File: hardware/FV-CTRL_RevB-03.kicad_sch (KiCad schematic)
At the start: 12 parts, among them J20 SMA 50ohm ANT, Y1 40MHz CL10pF

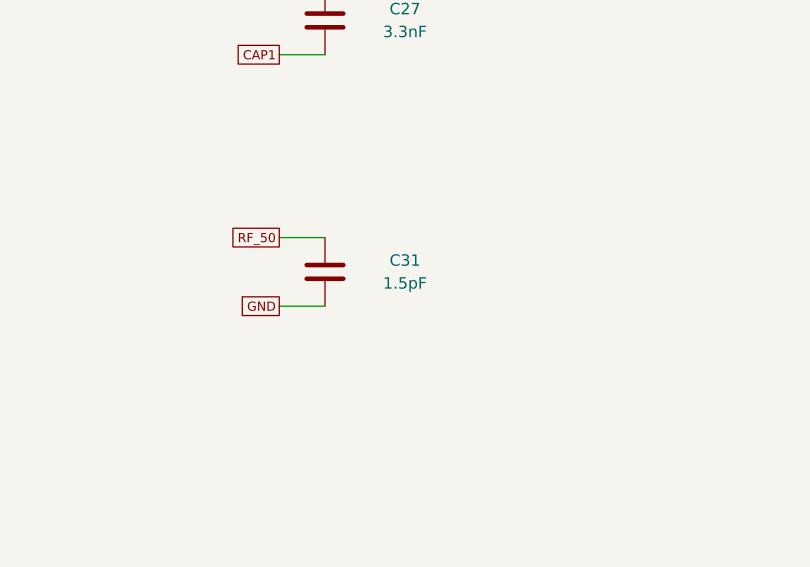
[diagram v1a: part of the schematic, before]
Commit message: fix(hardware): increase flash brownout margin and account for RF ESD capacitance
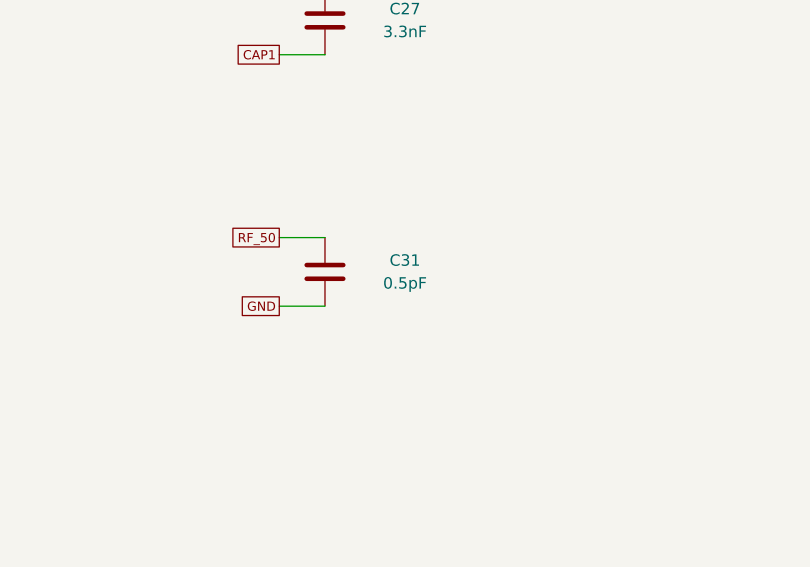
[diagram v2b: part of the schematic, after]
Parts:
- C31: value 1.5pF -> 0.5pF
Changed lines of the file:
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@@
 			(effects (font (size 1.27 1.27)))
 		)
-		(property "Value" "1.5pF"
+		(property "Value" "0.5pF"
 			(at 161.2900 97.7900 0)
 			(effects (font (size 1.27 1.27)))

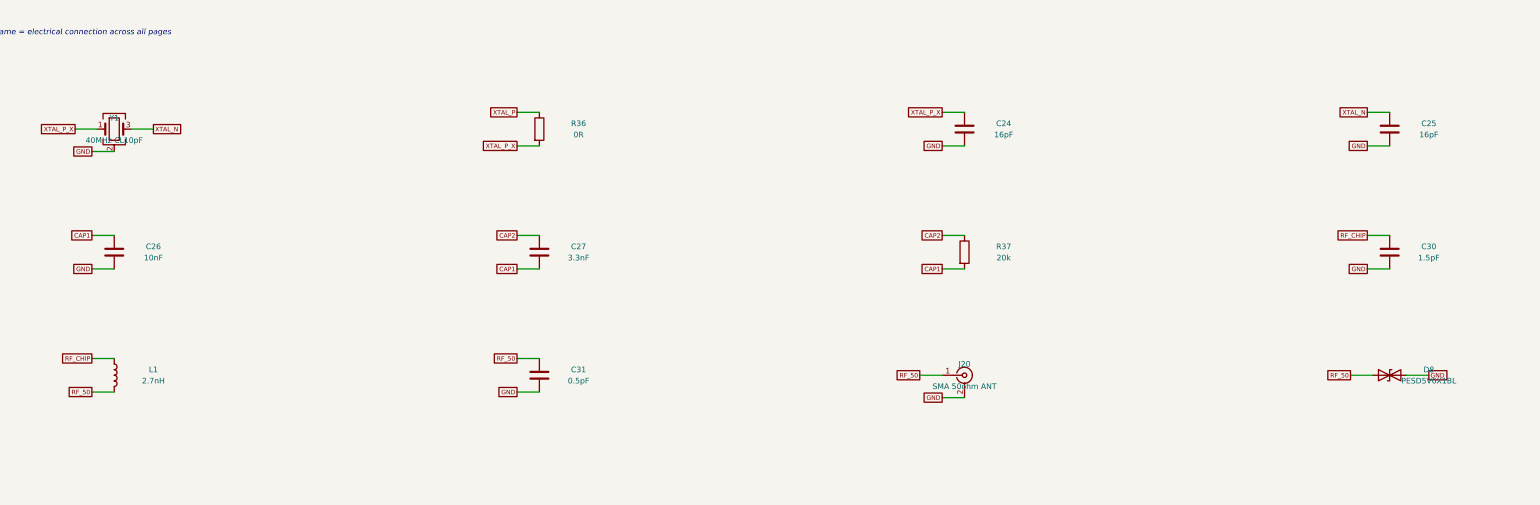
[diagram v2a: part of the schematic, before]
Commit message: feat(pcb): order QFN escapes and reconnect local supplies before signal routing
Keep two servo rails and GPIO unchanged. Use 0.4/0.2mm escape vias, move C23 to 0201 and preserve ground beneath clock/RF. ERC has zero violations; native DRC has no physical errors or parity differences, with 100 opens and 33 dangling warnings at this intermediate checkpoint. Not a fabrication release.
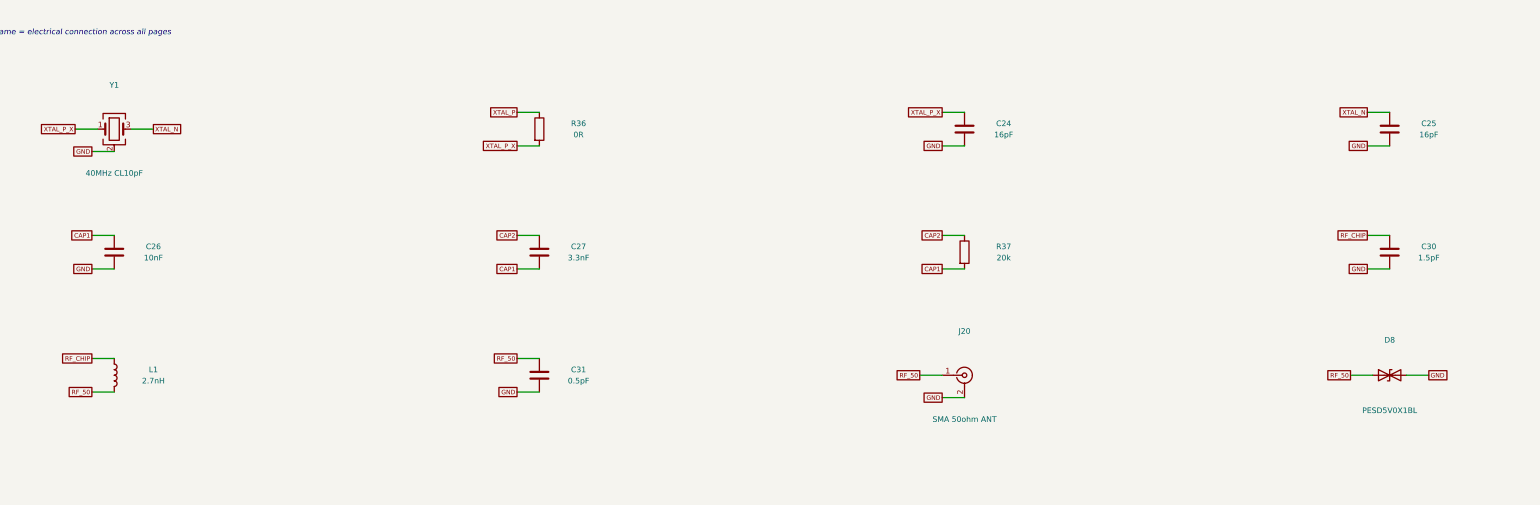
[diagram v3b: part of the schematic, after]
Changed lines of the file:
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@@
 		(dnp no)
 		(property "Reference" "Y1"
-			(at 55.8800 38.1000 0)
+			(at 55.8800 30.6400 0)
 			(effects (font (size 1.27 1.27)))
 		)
 		(property "Value" "40MHz CL10pF"
-			(at 55.8800 43.1800 0)
+			(at 55.8800 50.6400 0)
 			(effects (font (size 1.27 1.27)))
 		)
@@
 		(dnp no)
 		(property "Reference" "J20"
-			(at 248.9200 93.9800 0)
+			(at 248.9200 86.5200 0)
 			(effects (font (size 1.27 1.27)))
 		)
 		(property "Value" "SMA 50ohm ANT"
-			(at 248.9200 99.0600 0)
+			(at 248.9200 106.5200 0)
 			(effects (font (size 1.27 1.27)))
 		)
@@
 		(dnp no)
 		(property "Reference" "D8"
-			(at 354.3300 95.2500 0)
+			(at 345.4400 88.5200 0)
 			(effects (font (size 1.27 1.27)))
 		)
 		(property "Value" "PESD5V0X1BL"
-			(at 354.3300 97.7900 0)
-			(effects (font (size 1.27 1.27)))
-		)
+			(at 345.4400 104.5200 0)
+			(effects (font (size 1.27 1.27)))
+		)
